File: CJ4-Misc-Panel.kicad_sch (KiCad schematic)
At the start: 36 parts, among them J4 TC2030-IDC-NL, SW1 SW_PUSH_LED, SW10 SW_PUSH_LED, SW11 SW_PUSH_LED, SW12 SW_PUSH_LED, SW13 SW_PUSH_LED, SW14 SW_PUSH_LED, SW15 SW_PUSH_LED, SW16 SW_PUSH_LED, SW17 SW_PUSH_LED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

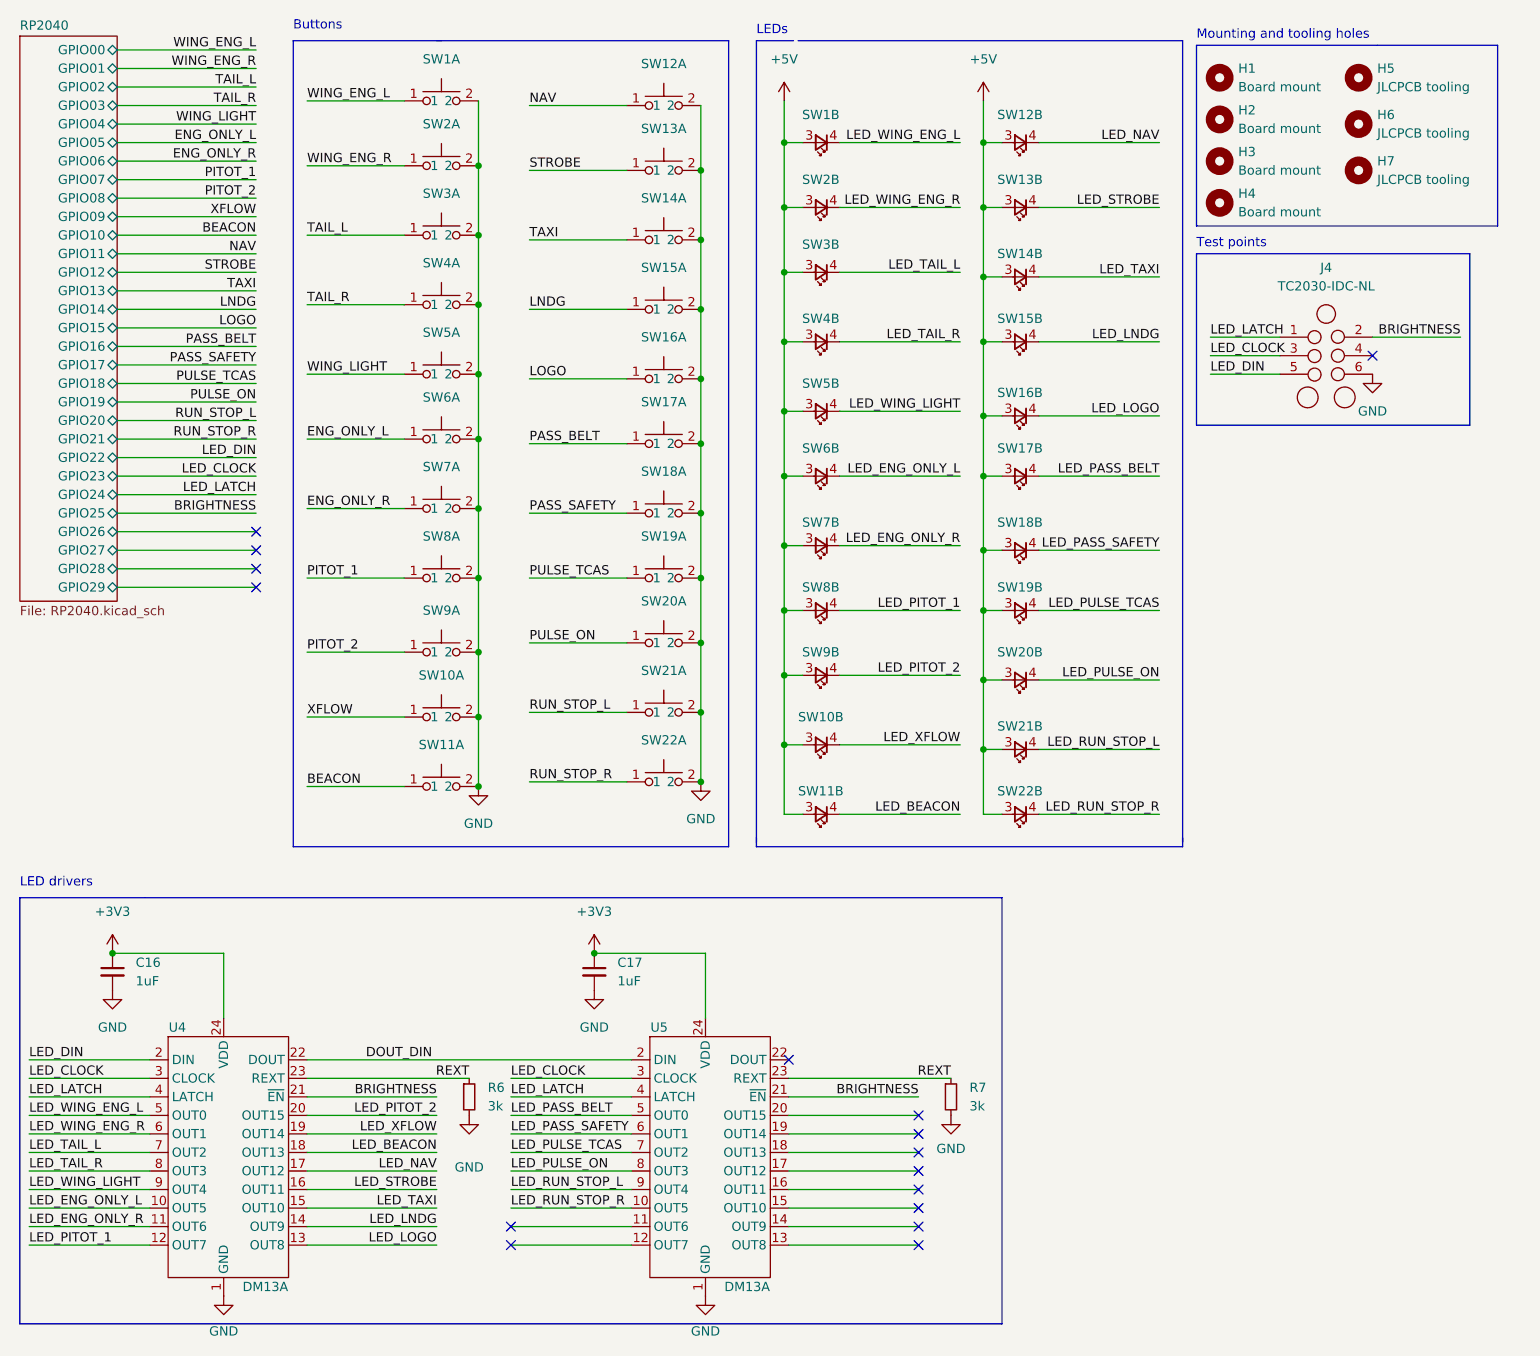
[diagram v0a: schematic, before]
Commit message: All the buttons are routed. Ugly, but routed.
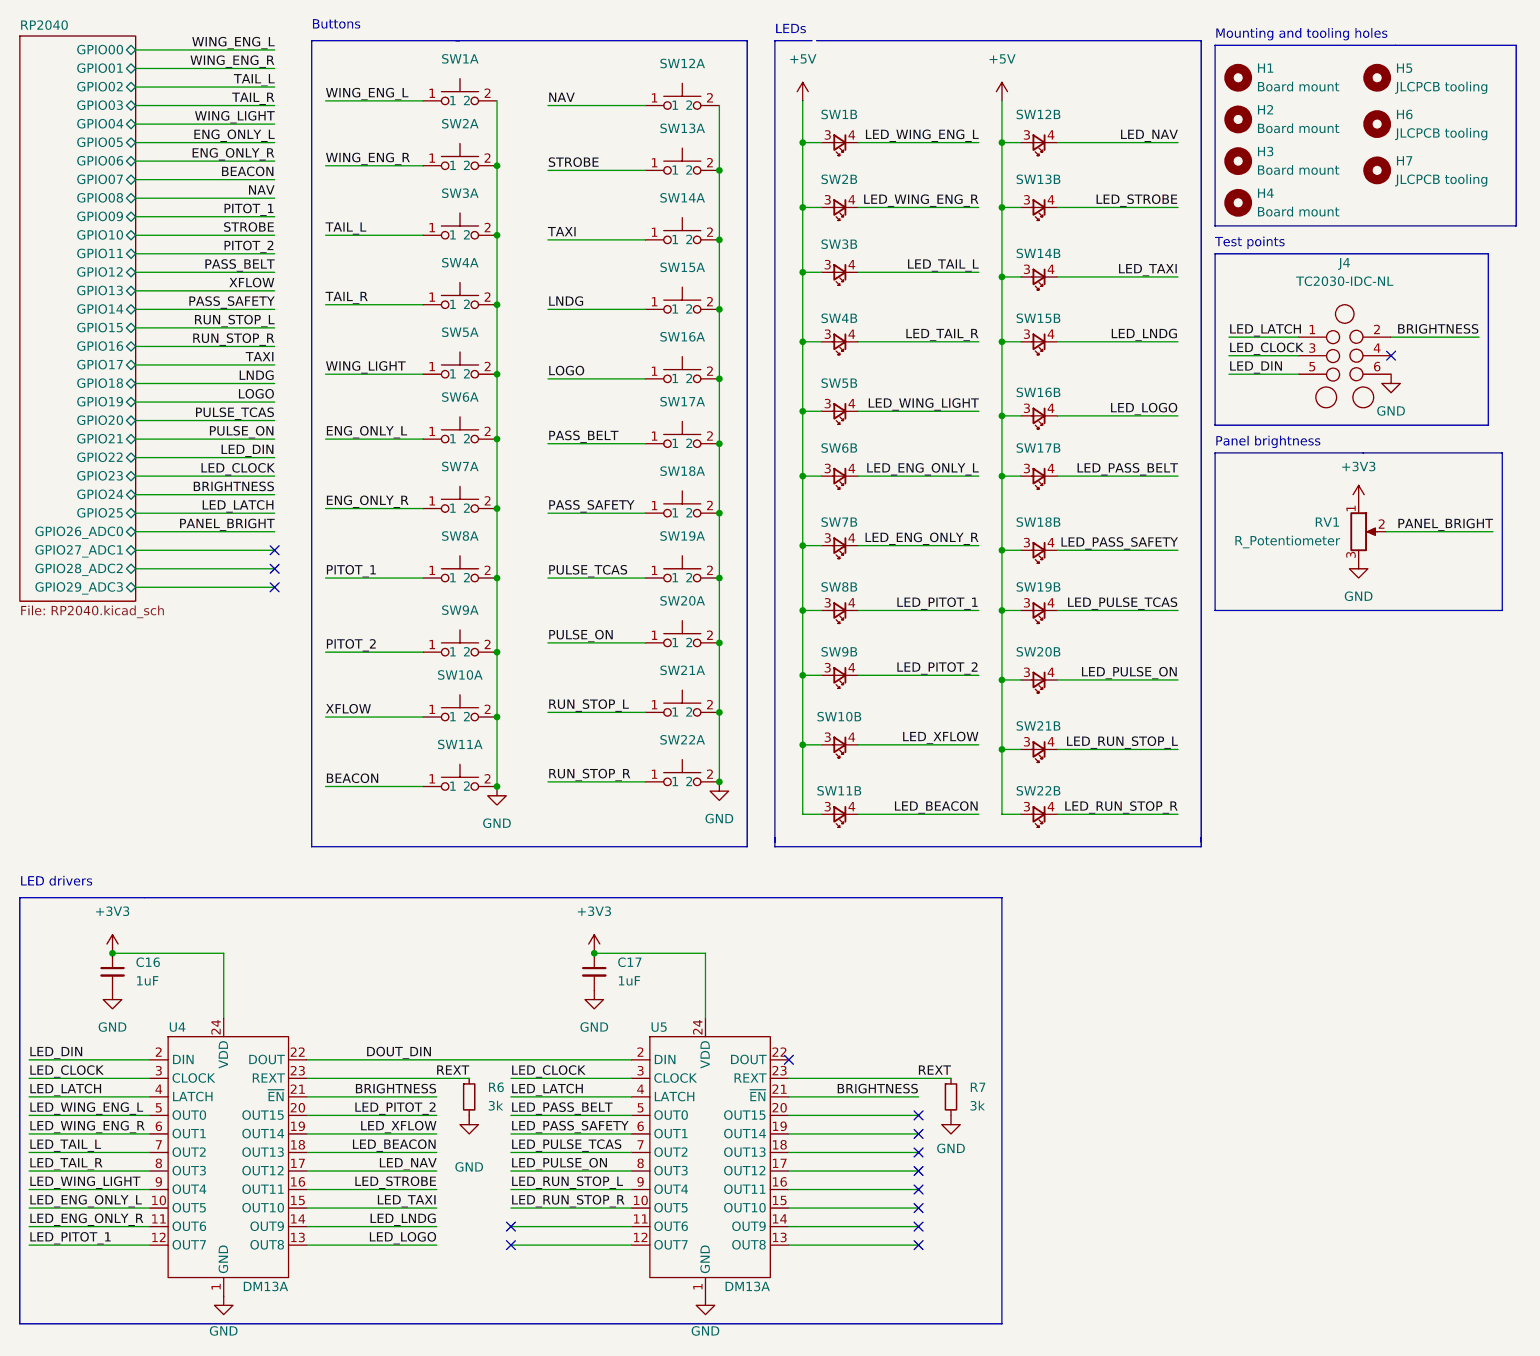
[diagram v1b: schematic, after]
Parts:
- removed J4: TC2030-IDC-NL, Connector:Tag-Connect_TC2030-IDC-NL_2x03_P1.27mm_Vertical, symbol Tag-Connect:TC2030-IDC-NL
- added J4: TC2030-IDC-NL, Connector:Tag-Connect_TC2030-IDC-NL_2x03_P1.27mm_Vertical, symbol Custom_Symbols:TC2030-IDC-NL
- added RV1: R_Potentiometer, Potentiometer_THT:Potentiometer_Bourns_PTV09A-1_Single_Vertical, symbol Device:R_Potentiometer
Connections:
- net +3V3: now also RV1.1
- net BRIGHTNESS: now also J4.2 (Pin_2)
- net GND: now also J4.6 (Pin_6), RV1.3
- net LED_CLOCK: now also J4.3 (Pin_3)
- net LED_DIN: now also J4.5 (Pin_5)
- net LED_LATCH: now also J4.1 (Pin_1)
- new net PANEL_BRIGHT: RV1.2
- no-connect marks 16 -> 15
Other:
- sheet RP2040 ports: added GPIO26_ADC0, GPIO27_ADC1, GPIO28_ADC2, GPIO29_ADC3; removed GPIO26, GPIO27, GPIO28, GPIO29
- note added: "Panel brightness"
- moved on the sheet: H1, H2, H3, H4, H5, H6, H7, SW10A, SW10B, SW11A, SW11B, SW12A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

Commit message: Fully routed!!!
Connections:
- net GND: now also J4.5 (Pin_5); no longer J4.6 (Pin_6)
- net LED_BEACON: now also U5.14 (OUT9); no longer U4.18 (OUT13)
- net LED_CLOCK: now also J4.4 (Pin_4); no longer J4.3 (Pin_3)
- net LED_DIN: now also J4.1 (Pin_1); no longer J4.5 (Pin_5)
- net LED_ENG_ONLY_L: now also U5.19 (OUT14); no longer U4.10 (OUT5)
- net LED_ENG_ONLY_R: now also U5.20 (OUT15); no longer U4.11 (OUT6)
- net LED_LATCH: now also J4.6 (Pin_6); no longer J4.1 (Pin_1)
- net LED_LNDG: now also U4.13 (OUT8); no longer U4.14 (OUT9)
- net LED_LOGO: now also U4.17 (OUT12); no longer U4.13 (OUT8)
- net LED_NAV: now also U5.15 (OUT10); no longer U4.17 (OUT12)
- net LED_PASS_BELT: now also U5.17 (OUT12); no longer U5.5 (OUT0)
- net LED_PASS_SAFETY: now also U5.18 (OUT13); no longer U5.6 (OUT1)
- net LED_PITOT_1: now also U5.12 (OUT7); no longer U4.12 (OUT7)
- net LED_PITOT_2: now also U5.8 (OUT3); no longer U4.20 (OUT15)
- net LED_PULSE_ON: now also U4.19 (OUT14); no longer U5.8 (OUT3)
- net LED_PULSE_TCAS: now also U4.18 (OUT13); no longer U5.7 (OUT2)
- net LED_RUN_STOP_L: now also U4.16 (OUT11); no longer U5.9 (OUT4)
- net LED_RUN_STOP_R: now also U4.15 (OUT10); no longer U5.10 (OUT5)
- net LED_STROBE: now also U5.16 (OUT11); no longer U4.16 (OUT11)
- net LED_TAIL_L: now also U5.9 (OUT4); no longer U4.7 (OUT2)
- net LED_TAIL_R: now also U5.7 (OUT2); no longer U4.8 (OUT3)
- net LED_TAXI: now also U4.14 (OUT9); no longer U4.15 (OUT10)
- net LED_WING_ENG_L: now also U5.11 (OUT6); no longer U4.5 (OUT0)
- net LED_WING_ENG_R: now also U5.10 (OUT5); no longer U4.6 (OUT1)
- net LED_WING_LIGHT: now also U5.5 (OUT0); no longer U4.9 (OUT4)
- net LED_XFLOW: now also U5.6 (OUT1); no longer U4.19 (OUT14)
- net REXT renamed REXT_1
- net REXT_1: no longer R7.1, U5.23 (REXT)
- new net REXT_2: R7.1, U5.23 (REXT)

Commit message: Cleanly routed
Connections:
- net LED_BEACON: now also U4.9 (OUT4); no longer U5.14 (OUT9)
- net LED_ENG_ONLY_L: now also U4.5 (OUT0); no longer U5.19 (OUT14)
- net LED_ENG_ONLY_R: now also U4.6 (OUT1); no longer U5.20 (OUT15)
- net LED_NAV: now also U4.10 (OUT5); no longer U5.15 (OUT10)
- net LED_PASS_BELT: now also U4.8 (OUT3); no longer U5.17 (OUT12)
- net LED_PASS_SAFETY: now also U4.7 (OUT2); no longer U5.18 (OUT13)
- net LED_PITOT_1: now also U5.11 (OUT6); no longer U5.12 (OUT7)
- net LED_STROBE: now also U4.11 (OUT6); no longer U5.16 (OUT11)
- net LED_TAIL_L: now also U5.12 (OUT7); no longer U5.9 (OUT4)
- net LED_WING_ENG_L: now also U5.10 (OUT5); no longer U5.11 (OUT6)
- net LED_WING_ENG_R: now also U5.9 (OUT4); no longer U5.10 (OUT5)
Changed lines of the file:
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@@
   (junction (at 80.01 63.5) (diameter 0) (color 0 0 0 0)
   )
+  (no_connect (at 137.795 165.1))
   (no_connect (at 15.875 182.88))
-  (no_connect (at 15.875 170.18))
+  (no_connect (at 137.795 167.64))
+  (no_connect (at 137.795 175.26))
+  (no_connect (at 137.795 177.8))
   (no_connect (at 49.53 90.17))
-  (no_connect (at 15.875 177.8))
-  (no_connect (at 15.875 167.64))
-  (no_connect (at 15.875 180.34))
+  (no_connect (at 137.795 170.18))
+  (no_connect (at 137.795 180.34))
   (no_connect (at 120.015 157.48))
   (no_connect (at 189.865 60.96))
-  (no_connect (at 15.875 172.72))
   (no_connect (at 71.755 165.1))
-  (no_connect (at 15.875 165.1))
+  (no_connect (at 137.795 172.72))
   (no_connect (at 49.53 92.71))
-  (no_connect (at 15.875 175.26))
   (no_connect (at 49.53 87.63))
   (no_connect (at 137.795 182.88))
@@
     (effects (font (size 1.27 1.27)) (justify right bottom))
   )
-  (label "LED_BEACON" (at 137.795 180.34 180)
-    (effects (font (size 1.27 1.27)) (justify right bottom))
+  (label "LED_BEACON" (at 15.875 175.26 0)
+    (effects (font (size 1.27 1.27)) (justify left bottom))
   )
   (label "BEACON" (at 56.515 120.015 0)
@@
     (effects (font (size 1.27 1.27)) (justify right bottom))
   )
-  (label "LED_ENG_ONLY_R" (at 137.795 165.1 180)
-    (effects (font (size 1.27 1.27)) (justify right bottom))
+  (label "LED_ENG_ONLY_L" (at 15.875 165.1 0)
+    (effects (font (size 1.27 1.27)) (justify left bottom))
   )
   (label "XFLOW" (at 56.515 110.49 0)
@@
     (effects (font (size 1.27 1.27)) (justify right bottom))
   )
+  (label "ENG_ONLY_L" (at 49.53 34.29 180)
+    (effects (font (size 1.27 1.27)) (justify right bottom))
+  )
   (label "WING_ENG_L" (at 49.53 19.05 180)
     (effects (font (size 1.27 1.27)) (justify right bottom))
@@
     (effects (font (size 1.27 1.27)) (justify right bottom))
   )
+  (label "BEACON" (at 49.53 31.75 180)
+    (effects (font (size 1.27 1.27)) (justify right bottom))
+  )
   (label "LED_STROBE" (at 173.355 40.64 180)
     (effects (font (size 1.27 1.27)) (justify right bottom))
@@
     (effects (font (size 1.27 1.27)) (justify right bottom))
   )
-  (label "LED_STROBE" (at 137.795 175.26 180)
-    (effects (font (size 1.27 1.27)) (justify right bottom))
-  )
-  (label "LED_PASS_SAFETY" (at 137.795 170.18 180)
-    (effects (font (size 1.27 1.27)) (justify right bottom))
+  (label "LED_STROBE" (at 15.875 180.34 0)
+    (effects (font (size 1.27 1.27)) (justify left bottom))
+  )
+  (label "LED_PASS_SAFETY" (at 15.875 170.18 0)
+    (effects (font (size 1.27 1.27)) (justify left bottom))
   )
   (label "LED_PITOT_2" (at 146.05 104.775 180)
@@
     (effects (font (size 1.27 1.27)) (justify left bottom))
   )
-  (label "ENG_ONLY_L" (at 49.53 31.75 180)
-    (effects (font (size 1.27 1.27)) (justify right bottom))
-  )
   (label "REXT_1" (at 76.2 160.02 180)
     (effects (font (size 1.27 1.27)) (justify right bottom))
@@
     (effects (font (size 1.27 1.27)) (justify right bottom))
   )
-  (label "LED_ENG_ONLY_L" (at 137.795 167.64 180)
-    (effects (font (size 1.27 1.27)) (justify right bottom))
+  (label "LED_ENG_ONLY_R" (at 15.875 167.64 0)
+    (effects (font (size 1.27 1.27)) (justify left bottom))
   )
   (label "LED_RUN_STOP_L" (at 71.755 175.26 180)
@@
     (effects (font (size 1.27 1.27)) (justify right bottom))
   )
-  (label "BEACON" (at 49.53 36.83 180)
-    (effects (font (size 1.27 1.27)) (justify right bottom))
-  )
   (label "LED_LATCH" (at 49.53 82.55 180)
     (effects (font (size 1.27 1.27)) (justify right bottom))
   )
-  (label "LED_TAIL_L" (at 81.915 175.26 0)
+  (label "LED_TAIL_L" (at 81.915 182.88 0)
     (effects (font (size 1.27 1.27)) (justify left bottom))
   )
@@
     (effects (font (size 1.27 1.27)) (justify left bottom))
   )
-  (label "LED_WING_ENG_L" (at 81.915 180.34 0)
+  (label "LED_WING_ENG_R" (at 81.915 175.26 0)
     (effects (font (size 1.27 1.27)) (justify left bottom))
   )
@@
     (effects (font (size 1.27 1.27)) (justify right bottom))
   )
+  (label "ENG_ONLY_R" (at 49.53 36.83 180)
+    (effects (font (size 1.27 1.27)) (justify right bottom))
+  )
   (label "LED_TAIL_R" (at 81.915 170.18 0)
     (effects (font (size 1.27 1.27)) (justify left bottom))
@@
     (effects (font (size 1.27 1.27)) (justify right bottom))
   )
-  (label "LED_WING_ENG_R" (at 81.915 177.8 0)
+  (label "LED_WING_ENG_L" (at 81.915 177.8 0)
     (effects (font (size 1.27 1.27)) (justify left bottom))
   )
@@
     (effects (font (size 1.27 1.27)) (justify right bottom))
   )
-  (label "ENG_ONLY_R" (at 49.53 34.29 180)
-    (effects (font (size 1.27 1.27)) (justify right bottom))
-  )
-  (label "LED_NAV" (at 137.795 177.8 180)
-    (effects (font (size 1.27 1.27)) (justify right bottom))
+  (label "LED_NAV" (at 15.875 177.8 0)
+    (effects (font (size 1.27 1.27)) (justify left bottom))
   )
   (label "LED_PULSE_TCAS" (at 173.355 95.885 180)
@@
     (effects (font (size 1.27 1.27)) (justify right bottom))
   )
-  (label "LED_PASS_BELT" (at 137.795 172.72 180)
-    (effects (font (size 1.27 1.27)) (justify right bottom))
-  )
-  (label "LED_PITOT_1" (at 81.915 182.88 0)
+  (label "LED_PASS_BELT" (at 15.875 172.72 0)
+    (effects (font (size 1.27 1.27)) (justify left bottom))
+  )
+  (label "LED_PITOT_1" (at 81.915 180.34 0)
     (effects (font (size 1.27 1.27)) (justify left bottom))
   )
@@
   (symbol (lib_id "Custom_Symbols:SW_PUSH_LED") (at 74.93 35.56 0) (unit 1)
     (in_bom yes) (on_board yes) (fields_autoplaced)
-    (property "Reference" "SW3" (id 0) (at 74.93 38.735 0))
+    (property "Reference" "SW3" (id 0) (at 74.93 39.37 0))
     (property "Value" "SW_PUSH_LED" (id 1) (at 74.93 38.1 0)
       (effects (font (size 1.27 1.27)) hide)
